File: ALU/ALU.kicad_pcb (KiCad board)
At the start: 2 copper layers, 152.4 x 152.4 mm, 91 parts, among them J1 Conn_01x08_Male, J10 Conn_01x01_Male, J11 Conn_01x08_Male, J12 Conn_01x01_Male, J13 Conn_01x01_Male, J14 Conn_01x03_Male, J15 Conn_01x01_Male, J16 Conn_01x01_Male, J17 Conn_01x01_Male, J18 Conn_01x01_Male, J19 Conn_01x01_Male, J2 Conn_01x08_Male, J20 Conn_01x01_Male, J21 Conn_01x01_Male, J22 Conn_01x01_Male, J23 Conn_01x01_Male, J24 Conn_01x01_Male, J25 Conn_01x01_Male, J26 Conn_01x01_Male, J27 Conn_01x01_Male, J28 Conn_01x01_Male, J29 Conn_01x01_Male, J3 Conn_01x08_Male, J30 Conn_01x01_Male, J31 Conn_01x01_Male, J32 Conn_01x01_Male, J33 Conn_01x01_Male, J34 Conn_01x01_Male, J35 Conn_01x01_Male, J36 Conn_01x01_Male, J37 Conn_01x01_Male, J38 Conn_01x01_Male, J39 Conn_01x01_Male, J4 Conn_01x01_Male, J5 Conn_01x01_Male, J6 Conn_01x01_Male, J7 Screw_Terminal_01x02, J8 Conn_01x08_Male, J9 Conn_01x01_Male, U1 74HC245, U10 74HC245, U11 CMD, U12 CMD, U13 CMD, U14 CMD, U15 CMD, U16 74HC74, U17 74LS00, U18 74LS08, U19 74LS10, U2 CMD, U20 74LS257, U21 74LS138, U22 74LS10, U23 74HC74, U24 74HC245, U25 74LS138, U26 74HC74, U27 74LS08, U28 74LS257, U29 74LS175, U3 CMD, U4 CMD, U5 CMD, U6 CMD, U7 CMD, U8 74HC245, U9 74LS08

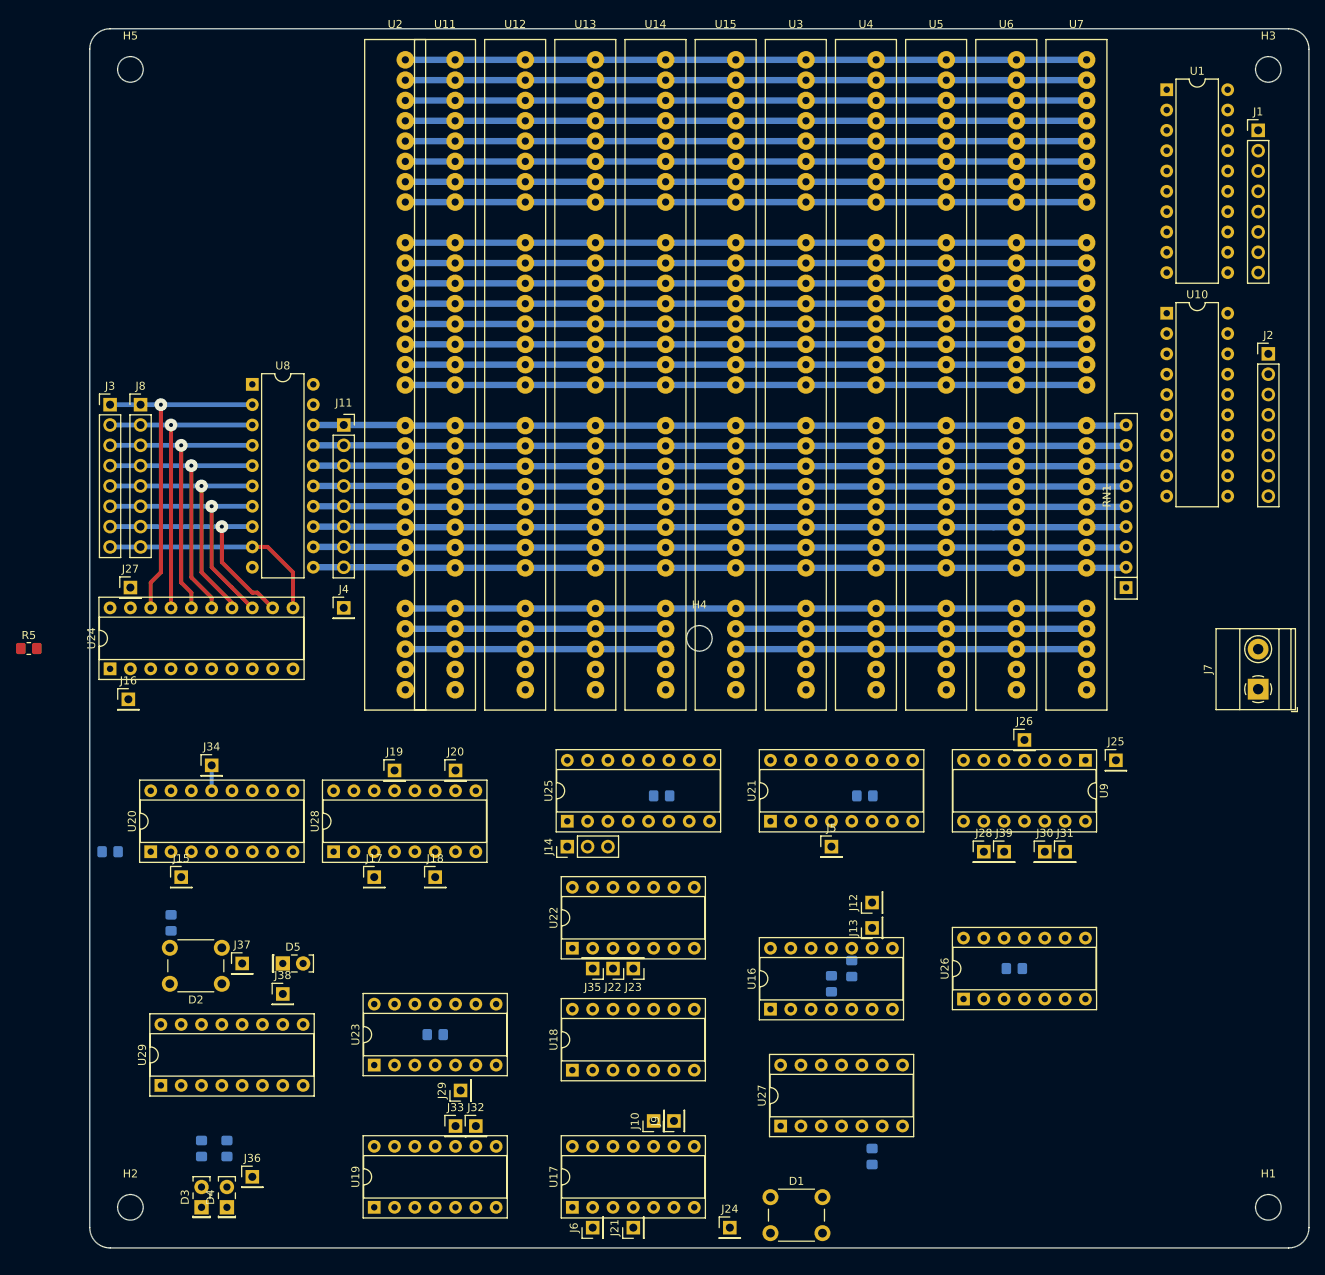
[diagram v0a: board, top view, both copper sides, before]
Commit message: Remove interrupt flag. Remove some logical items.
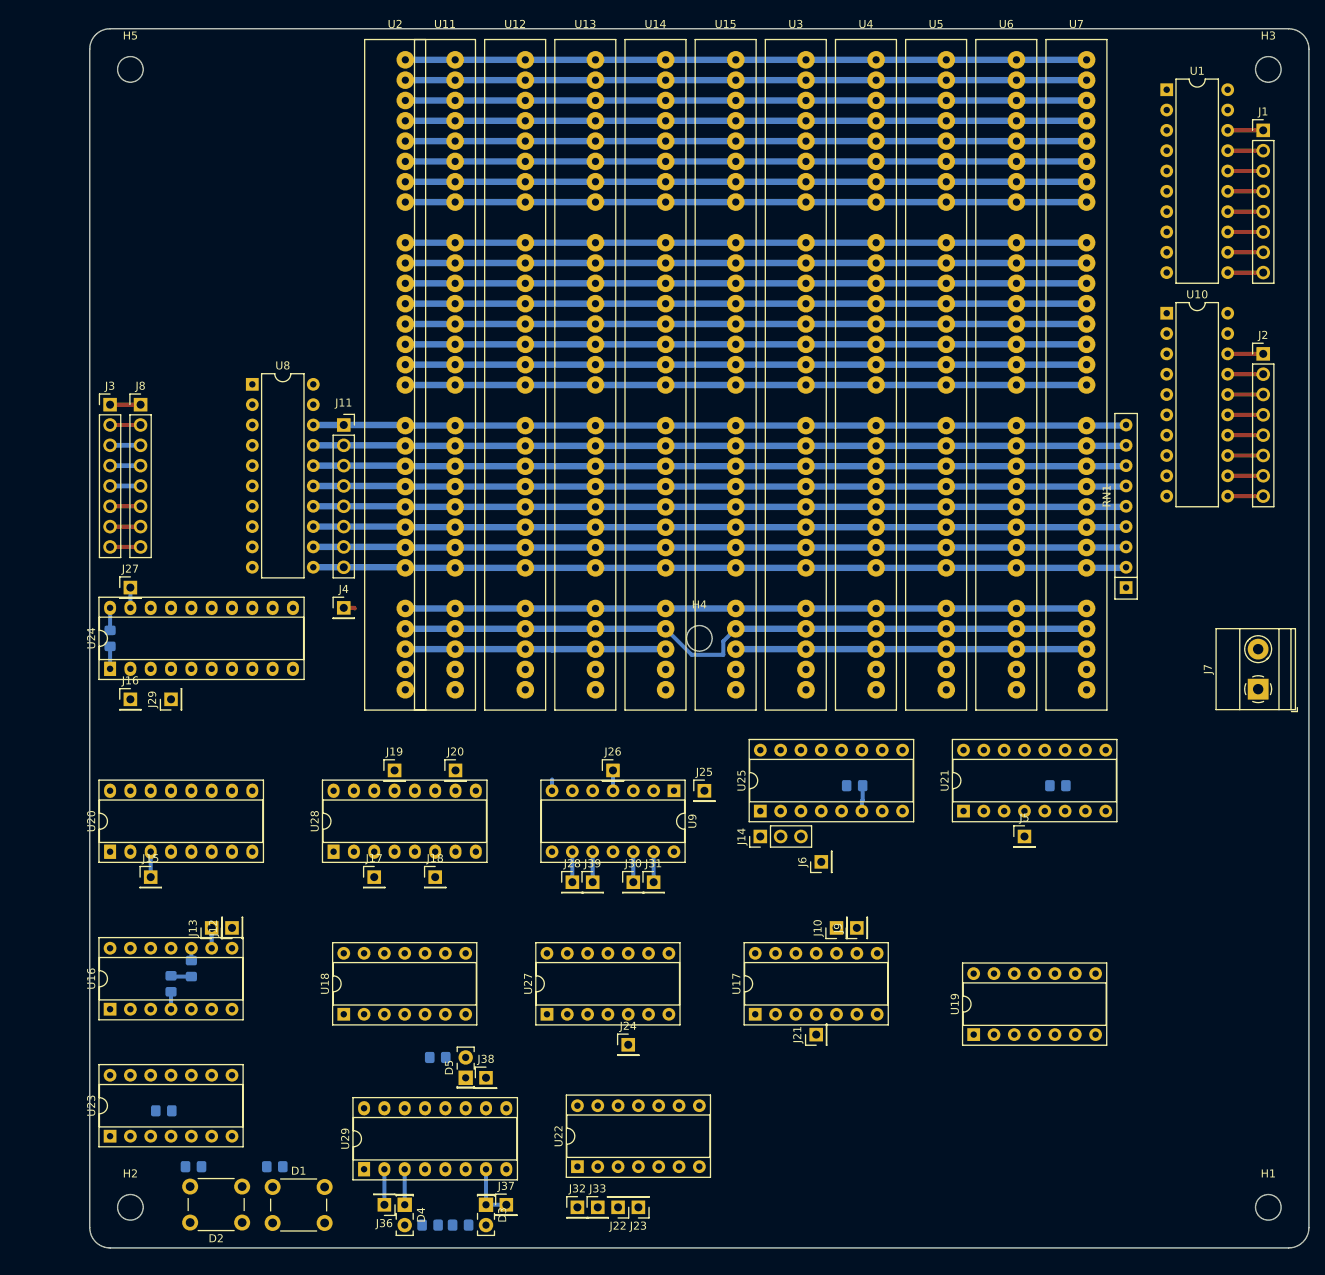
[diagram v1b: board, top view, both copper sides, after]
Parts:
- removed J34, J35: Conn_01x01_Male, Connector_PinHeader_2.54mm:PinHeader_1x01_P2.54mm_Vertical
- removed R3: 10k, Resistor_SMD:R_0805_2012Metric_Pad1.20x1.40mm_HandSolder
- removed U26: 74HC74, Package_DIP:DIP-14_W7.62mm_Socket
- R5: moved to B.Cu
- moved R9 107.8 mm to (41.0, 155.6)
- moved U16 82.6 mm to (34.3, 142.9)
- moved R1 82.5 mm to (41.9, 139.7)
- moved R2 82.5 mm to (44.5, 137.8)
- moved J13 82.5 mm to (47.0, 132.7)
- moved J12 80.1 mm to (49.5, 132.7)
- moved U19 78.0 mm to (142.2, 146.1)
- moved R6 74.7 mm to (54.9, 162.6), turned to 180 degrees
- moved D1 62.2 mm to (54.6, 165.1)
- moved J29 60.8 mm to (41.9, 104.1)
- moved J6 53.9 mm to (123.2, 124.5)
- moved J25 51.6 mm to (108.6, 115.6)
- moved J39 51.6 mm to (94.6, 127.0)
- moved J26 51.6 mm to (97.2, 113.0)
- moved J30 51.6 mm to (99.7, 127.0)
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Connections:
- U17 pad 1: /~ACT_BIN -> (no net)
- U17 pad 2: /~ACT_UNO -> (no net)
- U17 pad 3: Net-(U17-Pad3) -> (no net)
- U18 pad 9: Net-(U18-Pad9) -> /Arithm
- U19 pad 1: Net-(U17-Pad3) -> Net-(U19-Pad1)
- U19 pad 10: /~BANK1_CMD -> /~ACT_BIN
- U19 pad 11: /~POP_FL -> /~ACT_UNO
- U19 pad 8: Net-(U18-Pad12) -> Net-(U19-Pad1)
- U19 pad 9: /~BANK0_CMD -> /~ACT_BIN
- U20 pad 13: /~EI -> Net-(U20-Pad13)
- U20 pad 14: /BUS2 -> Net-(U20-Pad14)
- U22 pad 1: /~EI -> /~BANK0_CMD
- U22 pad 12: Net-(U18-Pad9) -> Net-(U18-Pad12)
- U22 pad 2: /~DI -> /~BANK1_CMD
- U23 pad 2: Net-(U20-Pad12) -> Net-(U23-Pad2)
- U23 pad 4: Net-(R3-Pad1) -> Net-(R9-Pad1)
- U23 pad 5: /IE -> Net-(U23-Pad5)
- U24 pad 6: Net-(U24-Pad6) -> Net-(U23-Pad5)
- U27 pad 1: /Arithm -> (no net)
- U27 pad 2: /C2 -> (no net)
- U27 pad 3: Net-(U26-Pad3) -> (no net)
- U28 pad 4: Net-(U26-Pad2) -> Net-(U23-Pad2)
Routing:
- net /BUS0: track 43.7 -> 3.81 mm, vias 1 -> 0
- net /BUS1: track 40.6 -> 3.81 mm, vias 1 -> 0
- net /BUS2: track 38.6 -> 3.81 mm, vias 1 -> 0
- net /BUS3: track 36.6 -> 3.81 mm, vias 1 -> 0
- net /BUS4: track 34.6 -> 4.44 mm, vias 1 -> 0
- net /BUS5: track 32.6 -> 3.81 mm, vias 1 -> 0
- net /BUS6: track 30.9 -> 3.81 mm, vias 1 -> 0
- net /BUS7: track 28.6 -> 3.81 mm
- net VCC: track 76.4 -> 94.2 mm
- net /~EQ_OUT: track 0.00 -> 6.98 mm
- net Net-(J2-Pad8): track 0.00 -> 4.44 mm
- net Net-(J2-Pad7): track 0.00 -> 4.44 mm
- net Net-(J2-Pad6): track 0.00 -> 4.44 mm
- net Net-(J2-Pad5): track 0.00 -> 4.44 mm
- net Net-(J2-Pad4): track 0.00 -> 4.44 mm
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
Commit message: Remove tracks, adjust sockets
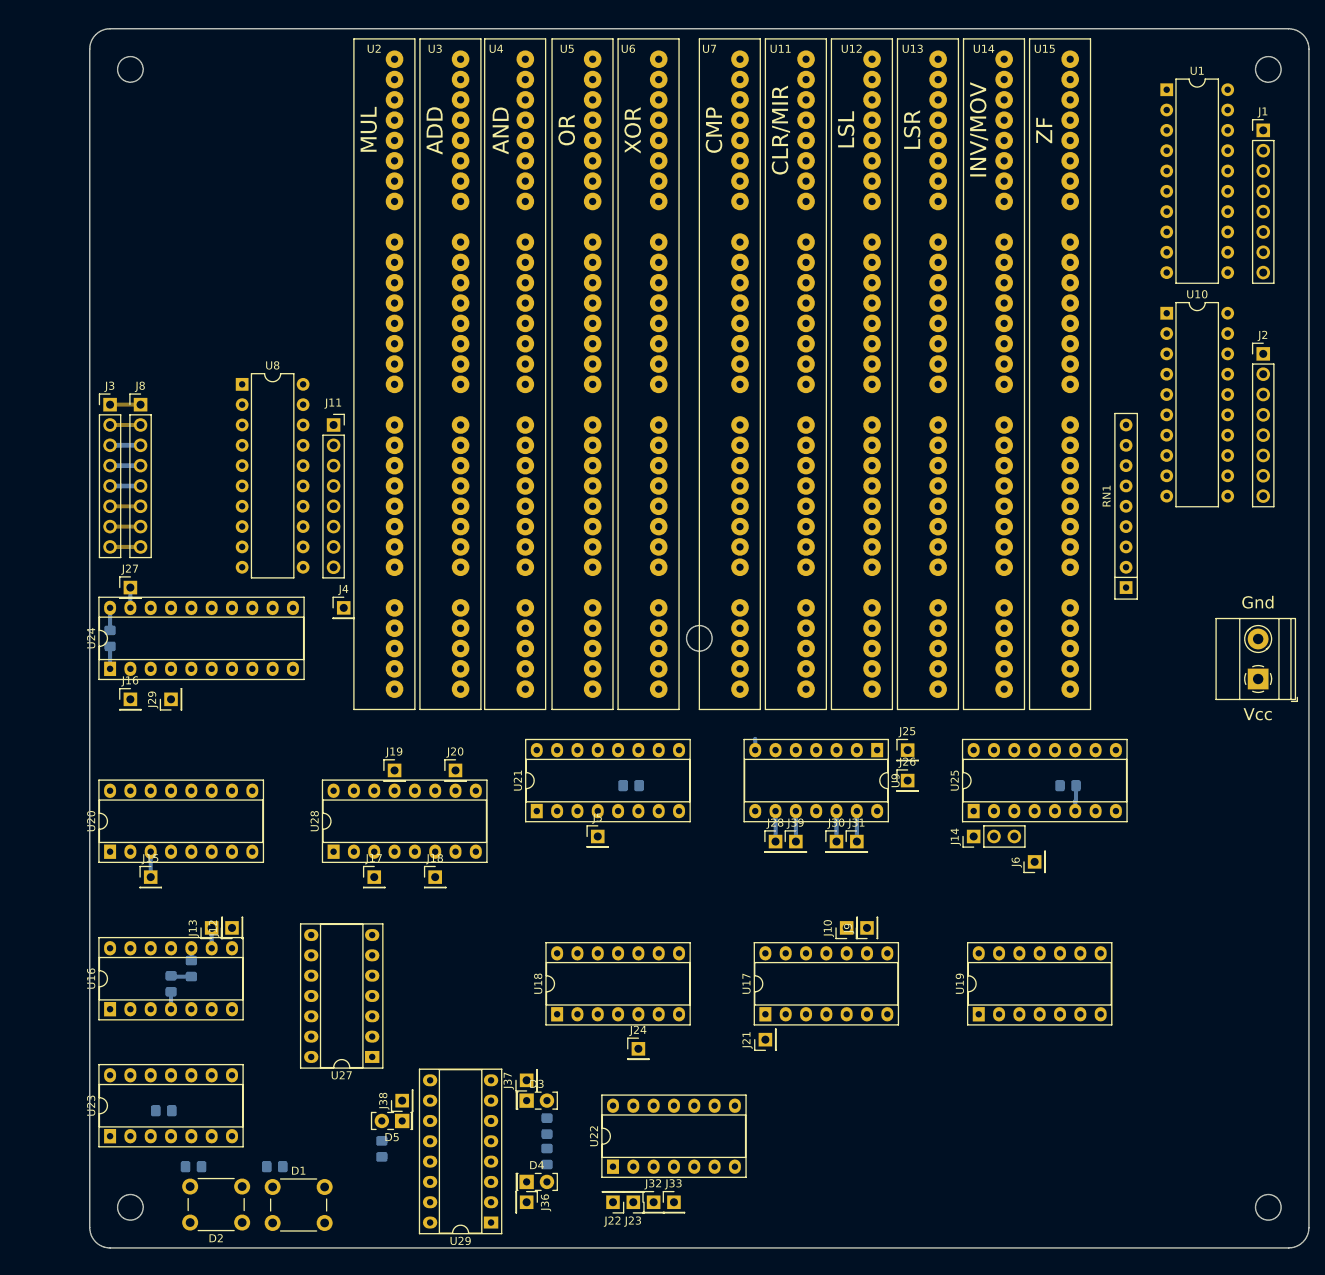
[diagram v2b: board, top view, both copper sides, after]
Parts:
- moved J5 53.3 mm to (95.2, 121.3)
- moved U21 53.3 mm to (87.6, 118.1)
- moved R4 53.3 mm to (99.4, 114.9)
- moved U6 44.7 mm to (102.9, 24.1)
- moved U5 44.2 mm to (94.6, 24.1)
- moved U11 43.9 mm to (121.3, 24.1)
- moved U4 43.9 mm to (86.2, 24.1)
- moved U12 43.3 mm to (129.5, 24.1)
- moved U7 43.3 mm to (113.0, 24.1)
- moved U3 43.2 mm to (78.1, 24.1)
- moved U13 42.8 mm to (137.8, 24.1)
- moved U14 42.3 mm to (146.1, 24.1)
- moved U15 41.8 mm to (154.3, 24.1)
- moved J26 36.9 mm to (134.0, 114.3)
- moved J14 26.7 mm to (142.2, 121.3)
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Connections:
- U17 pad 1: (no net) -> /~ADDx
- U17 pad 2: (no net) -> /~POP_FL
- U17 pad 3: (no net) -> Net-(U17-Pad3)
- U17 pad 4: /~ADDx -> (no net)
- U17 pad 5: /~POP_FL -> (no net)
- U17 pad 6: Net-(U17-Pad6) -> (no net)
- U18 pad 1: Net-(U17-Pad6) -> Net-(U18-Pad1)
- U18 pad 11: Net-(U18-Pad11) -> Net-(U16-Pad3)
- U18 pad 12: Net-(U18-Pad12) -> Net-(U17-Pad3)
- U18 pad 3: Net-(U16-Pad3) -> Net-(U18-Pad3)
- U22 pad 1: /~BANK0_CMD -> /~LSLx
- U22 pad 12: Net-(U18-Pad12) -> Net-(U18-Pad4)
- U22 pad 2: /~BANK1_CMD -> /~LSRx
- U22 pad 3: /~LSLx -> /~BANK0_CMD
- U22 pad 4: /~LSRx -> /~BANK1_CMD
- U22 pad 6: Net-(U18-Pad4) -> Net-(U18-Pad1)
- U23 pad 11: Net-(U18-Pad11) -> Net-(U18-Pad3)
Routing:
- net /O7: track 101.7 -> 0.11 mm
- net /O6: track 101.7 -> 0.11 mm
- net /O5: track 101.7 -> 0.11 mm
- net /O4: track 101.7 -> 0.11 mm
- net /O3: track 101.7 -> 0.11 mm
- net /O2: track 101.7 -> 0.11 mm
- net /O1: track 101.7 -> 0.11 mm
- net /O0: track 101.7 -> 0.11 mm
- net VCC: track 94.2 -> 5.39 mm
- net /Latch: track 86.6 -> 0.00 mm
- net /A4: track 85.2 -> 0.00 mm
- net /A3: track 85.2 -> 0.00 mm
- net /A2: track 85.2 -> 0.00 mm
- net /A1: track 85.2 -> 0.00 mm
- net /B7: track 85.2 -> 0.00 mm
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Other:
- board text added: "ADD"
- board text added: "AND"
- board text added: "CLR/MIR"
- board text added: "CMP"
- board text added: "Gnd"
- board text added: "INV/MOV"
- board text added: "LSL"
- board text added: "LSR"
- board text added: "MUL"
- board text added: "OR"
- board text added: "Vcc"
- board text added: "XOR"
- board text added: "ZF"

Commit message: Autorouted ALU
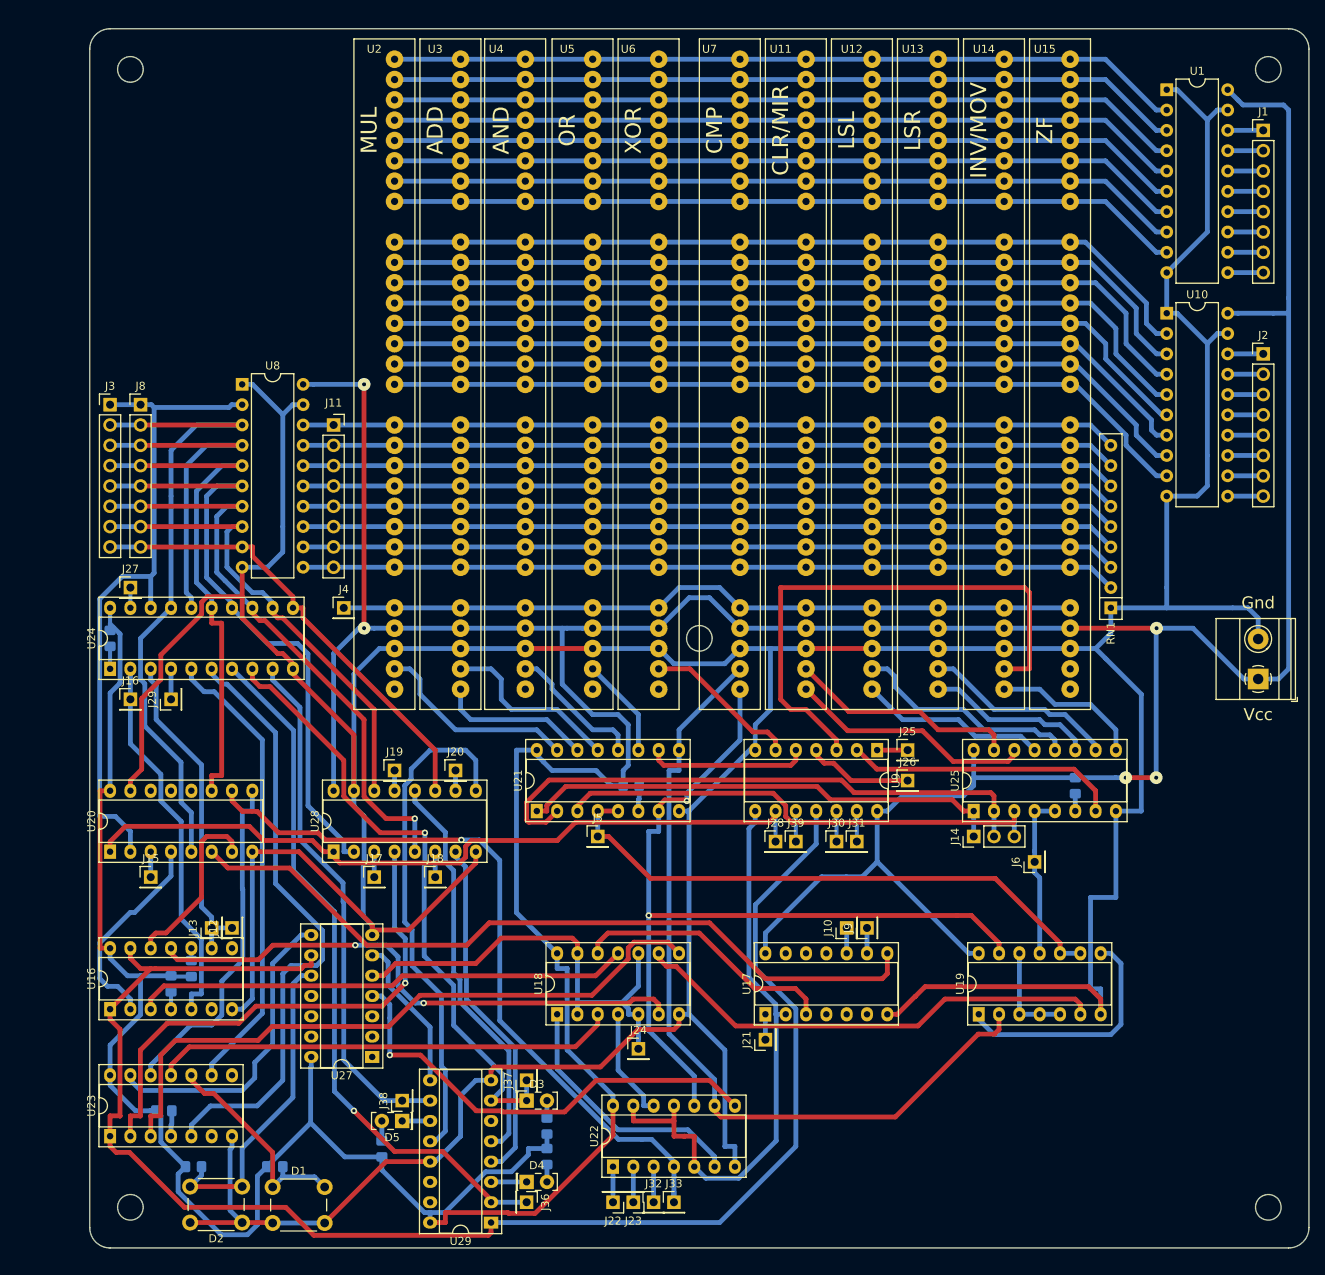
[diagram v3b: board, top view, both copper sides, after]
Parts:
- moved RN1 3.17 mm to (159.4, 92.7)
- moved R7 0.91 mm to (154.9, 114.9), turned to 90 degrees
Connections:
- U21 pad 13: /~ADDC -> /~ADD
- U21 pad 14: /~ADD -> /~ADDC
- U25 pad 10: /~LSRC -> /~LSR
- U25 pad 11: /~LSR -> /~LSRC
- U25 pad 12: /~LSLC -> /~LSL
- U25 pad 13: /~LSL -> /~LSLC
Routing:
- net VCC: track 5.39 -> 666.0 mm, vias 0 -> 5
- net GND: track 1.41 -> 648.1 mm
- net /~RES_FL: track 0.00 -> 194.8 mm
- net /~CMPC: track 0.00 -> 108.2 mm, vias 0 -> 2
- net /~CMP: track 0.00 -> 104.3 mm
- net /A2: track 0.00 -> 103.5 mm
- net /A3: track 0.00 -> 103.1 mm
- net /A1: track 0.00 -> 103.1 mm
- net /A0: track 0.00 -> 102.7 mm
- net /A4: track 0.00 -> 102.4 mm
- net /A7: track 0.00 -> 102.0 mm
- net /A6: track 0.00 -> 102.0 mm
- net /A5: track 0.00 -> 102.0 mm
- net /O5: track 0.11 -> 102.1 mm
- net /O0: track 0.11 -> 102.1 mm
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
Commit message: Polishing ALU
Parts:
- added J34: Conn_01x01_Male, Connector_PinHeader_2.54mm:PinHeader_1x01_P2.54mm_Vertical, F.Cu at (86.4, 151.8)
- added U26: 74LS27, Package_DIP:DIP-14_W7.62mm_Socket, F.Cu at (50.8, 39.4)
- moved J37 6.35 mm to (86.4, 158.1)
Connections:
- J37 pad 1: /~EQ_OUT -> /EQ_OUT
- U29 pad 6: Net-(U29-Pad6) -> /EQ_OUT
- U8 pad 19: GND -> Net-(U26-Pad8)
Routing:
- net (no net): track 0.00 -> 350.5 mm, vias 0 -> 180
- net /Arithm: track 59.8 -> 289.1 mm
- net /~OUT: track 3.81 -> 175.5 mm, vias 0 -> 1
- net /~XOUT: track 13.4 -> 149.9 mm, vias 0 -> 1
- net VCC: track 666.0 -> 696.5 mm, vias 5 -> 7
- net Net-(U14-Pad28): track 68.4 -> 49.2 mm, vias 0 -> 1
- net Net-(U26-Pad8): track 0.00 -> 16.7 mm
- net Net-(U26-Pad11): track 0.00 -> 12.7 mm
- net Net-(U26-Pad10): track 0.00 -> 8.15 mm
- net GND: track 648.1 -> 656.0 mm
- net /EQ_OUT: track 0.00 -> 4.97 mm
- net /~CMP: track 104.3 -> 107.1 mm
- net Net-(U6-Pad28): track 19.6 -> 21.0 mm
- net /~AND: track 17.3 -> 18.2 mm
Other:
- board text added: "ADD_CIN"
- board text added: "ADD_COUT"
- board text added: "Bank0"
- board text added: "Bank1"
- board text added: "C2"
- board text added: "COP[0-2]"
- board text added: "DST"
- board text added: "EQ"
- board text added: "EQ_OUT"
- board text added: "GT"
- board text added: "GT_OUT"
- board text added: "IE"
- board text added: "LSx_CIN"
- board text added: "LT"
- board text added: "LT_OUT"
- board text added: "Latch"
- board text added: "OUT BUS"
- board text added: "SRC"
- board text added: "~ACT_BIN"
- board text added: "~ACT_UNO"
- board text added: "~ADDx"
- board text added: "~BANK0_CMD"
- board text added: "~BANK1_CMD"
- board text added: "~CLRF"
- board text added: "~EQ"
- board text added: "~EQ_OUT"
- board text added: "~LSL_COUT"
- board text added: "~LSLx"
- board text added: "~LSR_COUT"
- board text added: "~LSRx"
- board text added: "~OUT"
- board text added: "~POPF"
- board text added: "~PUSHF"
- board text added: "~RESET"
- board text added: "~RETI"
- board text added: "~XOUT"

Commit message: Polishing ALU
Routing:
- net /~POP_FL: track 74.1 -> 81.3 mm
- net Net-(U18-Pad8): track 83.4 -> 86.9 mm
- net /~BANK1_CMD: track 93.4 -> 95.9 mm
- net Net-(U17-Pad3): track 33.2 -> 35.0 mm
- net Net-(U16-Pad3): track 62.1 -> 63.7 mm
- net GND: track 656.0 -> 657.7 mm
- net Net-(U23-Pad2): track 65.6 -> 66.7 mm
- net Net-(U17-Pad8): track 96.1 -> 97.2 mm
- net /~EQ_OUT: track 78.6 -> 79.5 mm
- net /~CMPC: track 108.2 -> 109.1 mm
- net Net-(U16-Pad2): track 26.0 -> 26.9 mm
- net Net-(U16-Pad12): track 22.3 -> 21.6 mm
- net Net-(U18-Pad4): track 14.0 -> 13.3 mm
- net /~RES_FL: track 194.8 -> 195.5 mm
- net Net-(U16-Pad11): track 69.6 -> 70.1 mm
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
